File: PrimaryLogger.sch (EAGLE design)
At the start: 67 parts, among them J1 CONN_42.54_SCREW, J2 CONN_42.54_SCREW, J3 CONN_42.54_SCREW, J4 CONN_42.54_SCREW, J5 CONN_32.54_SCREW, Q1 DMG3404, Q2 DMG3404, U1 MIC2005, U2 MIC2091, U25 SN74AUP3G34DCU, U3 TPL5010DDC, U4 TXS0102DCU, U5 SN74LVC1G3157SC70, U6 TCS3400, U7 SHTC3DFN, U8 MCP23008QFN, U9 MCP7940SOIC

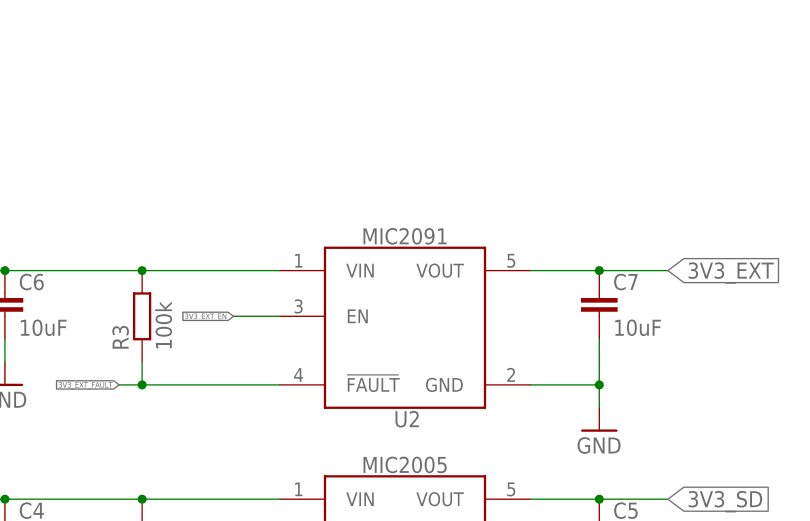
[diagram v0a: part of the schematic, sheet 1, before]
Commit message: Updated part numbers
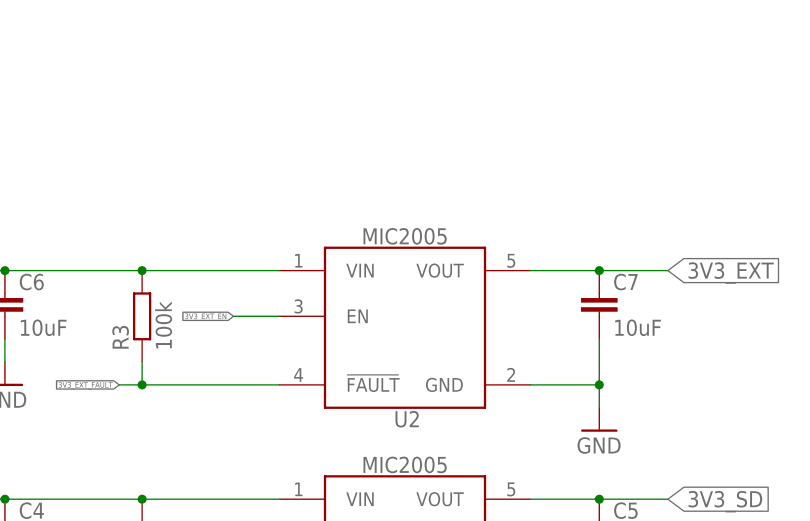
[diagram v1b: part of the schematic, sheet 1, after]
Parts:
- U2: value MIC2091 -> MIC2005; device bschulz:MIC2091 -> bschulz:MIC2005
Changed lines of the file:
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@@
 <part name="R2" library="bschulz_passives" deviceset="R-EU_" device="R0603" technology="100K" value="100k"/>
 <part name="GND7" library="supply1" library_urn="urn:adsk.eagle:library:371" deviceset="GND" device=""/>
-<part name="U2" library="bschulz" deviceset="MIC209*" device="" technology="1" value="MIC2091"/>
+<part name="U2" library="bschulz" deviceset="MIC2005" device="" value="MIC2005"/>
 <part name="C6" library="bschulz_passives" deviceset="C-EU" device="C0805" technology="10UF" value="10uF"/>
 <part name="C7" library="bschulz_passives" deviceset="C-EU" device="C0805" technology="10UF" value="10uF"/>

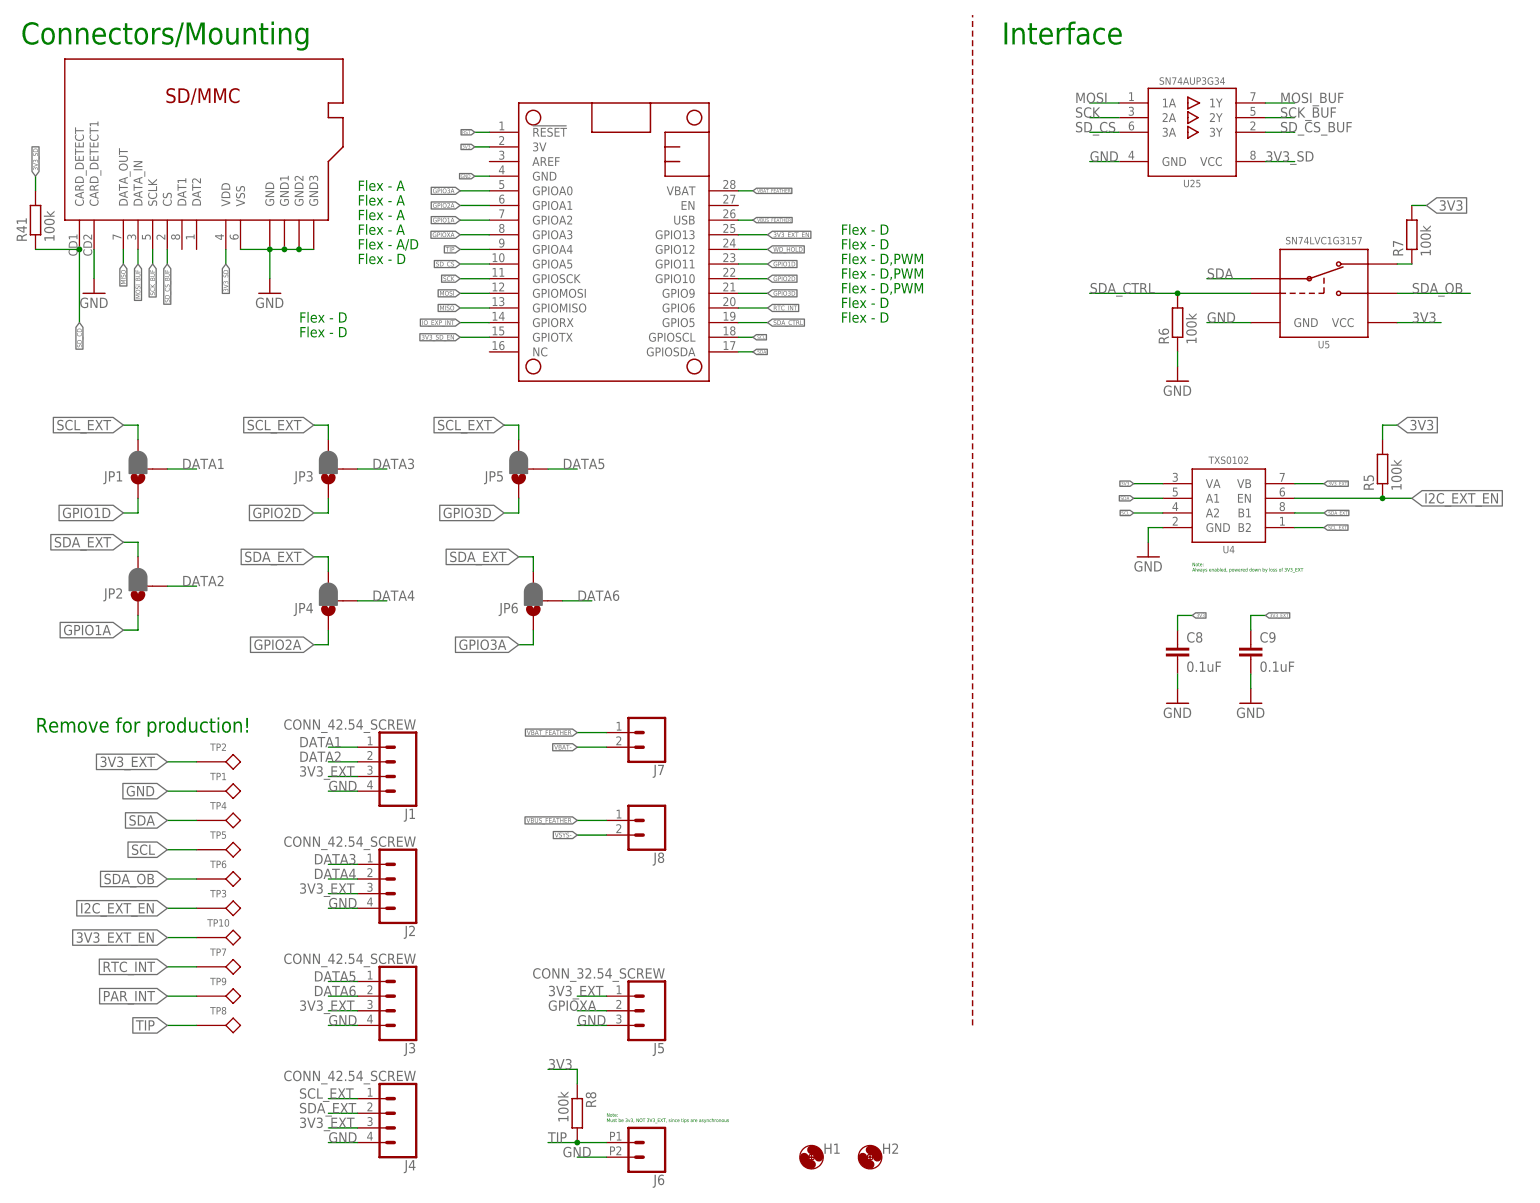
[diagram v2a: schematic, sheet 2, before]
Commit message: Updated parts for BoM, moved designators, changed R41
Updated part numbers to generate BoM, moved `R11` designator and changed `R41` to be `R12` to match ordering of rest of board (was carry over from Resnik I think)
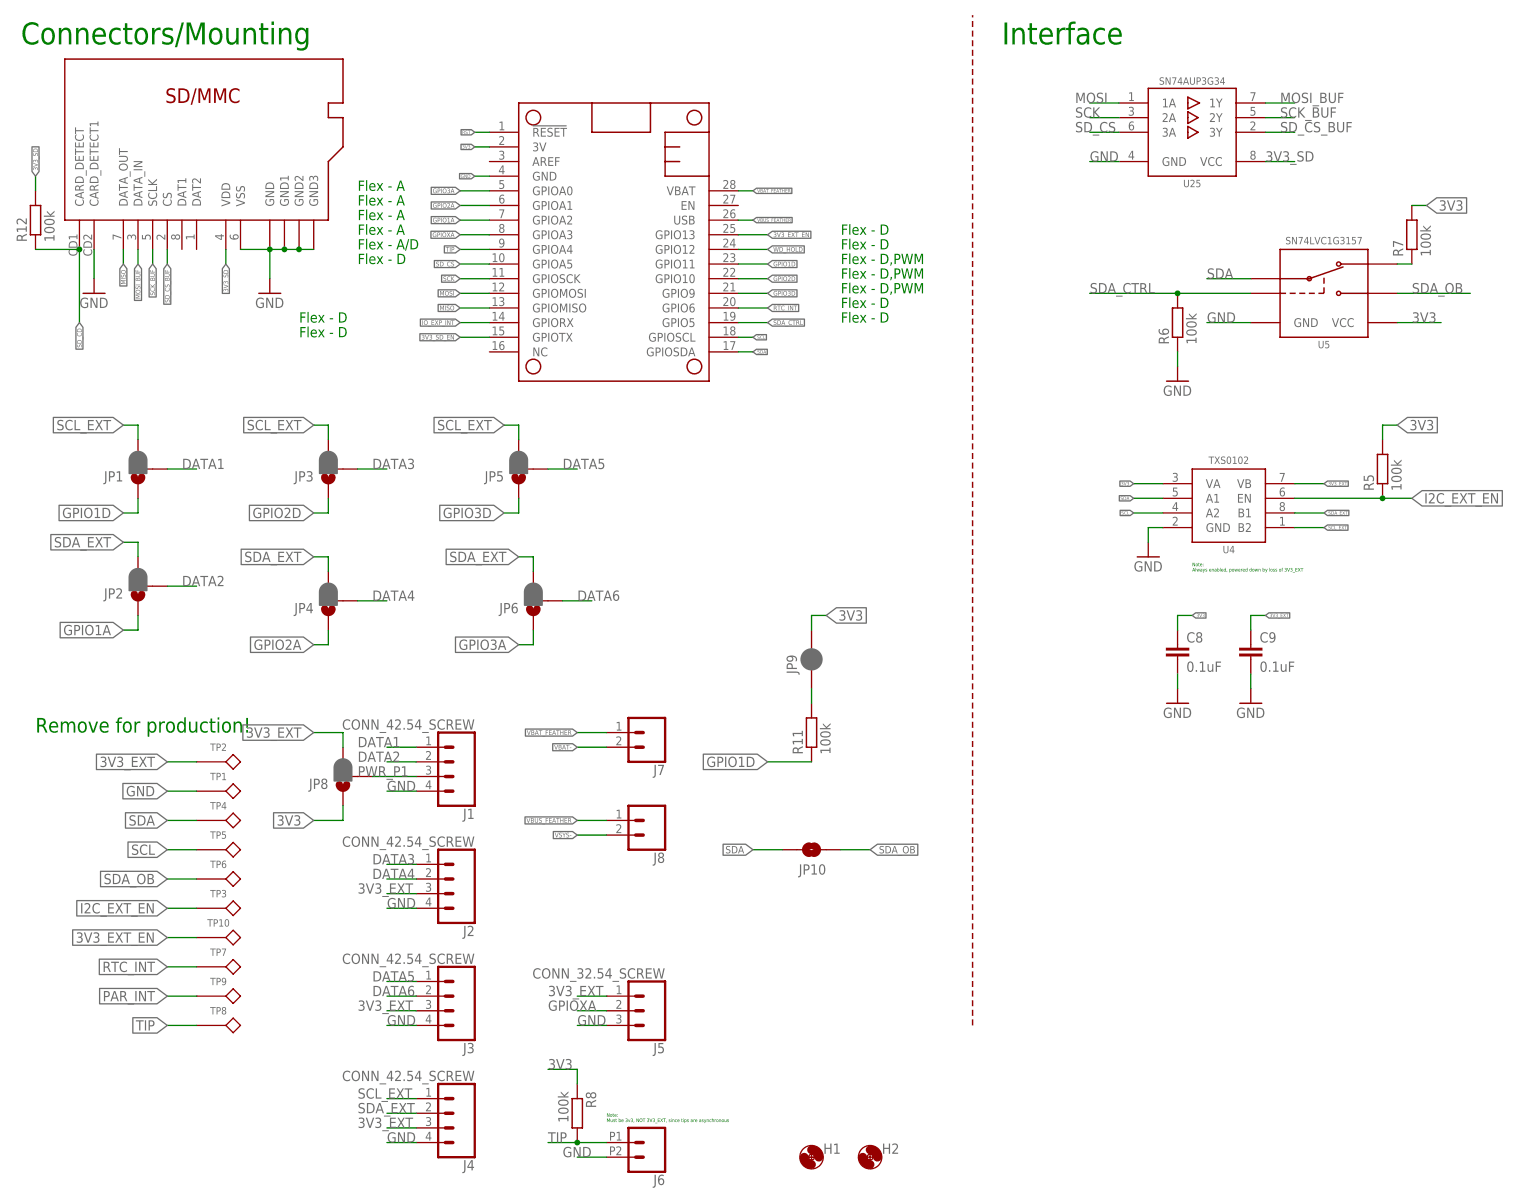
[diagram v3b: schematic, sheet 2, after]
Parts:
- added JP10: JUMPER-SMT_2_NO_SILK, SparkFun-Jumpers:JUMPER-SMT_2_NO_SILK
- added JP8: JUMPER-SMT_3_1-NC_PASTE_SILK, SparkFun-Jumpers:JUMPER-SMT_3_1-NC_PASTE_SILK
- added JP9: JUMPER-SMT_2_NC_PASTE_SILK, SparkFun-Jumpers:JUMPER-SMT_2_NC_PASTE_SILK
- added R11, R9: 100k, bschulz_passives:R-EU_100KR0603
- R8: device bschulz_passives:R-EU_100KR0603 -> bschulz_passives:R-EU_10KR0603
- renumbered R41 to R12
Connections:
- new net N$5: JP9.1, R11.2
- new net PWR_P1: J1.3, JP8.2
- net 3V3: now also JP8.1, JP9.2, R9.2
- net 3V3_EXT: now also JP8.3; no longer J1.3
- net GPIO1D: now also R11.1
- net RTC_INT: now also R9.1
- net SDA: now also JP10.2
- net SDA_OB: now also JP10.1
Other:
- moved on the sheet: J1, J2, J3, J4

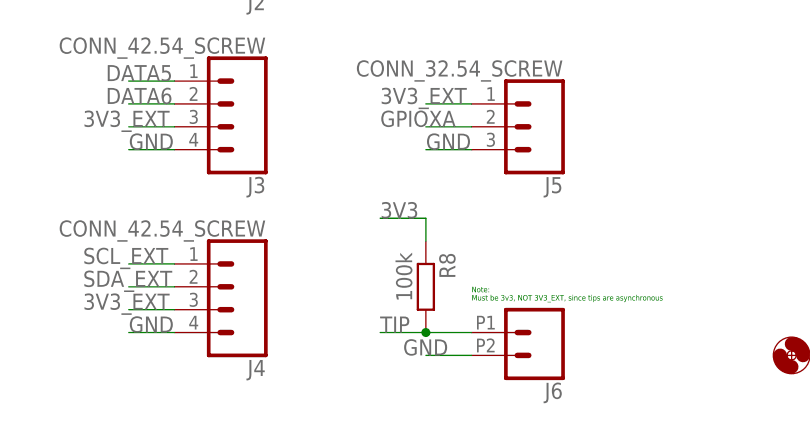
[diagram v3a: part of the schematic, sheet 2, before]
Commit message: Gerber and part updates
Added Gerber files for Advanced Circuits order, minor changes to part numbers and BoMs
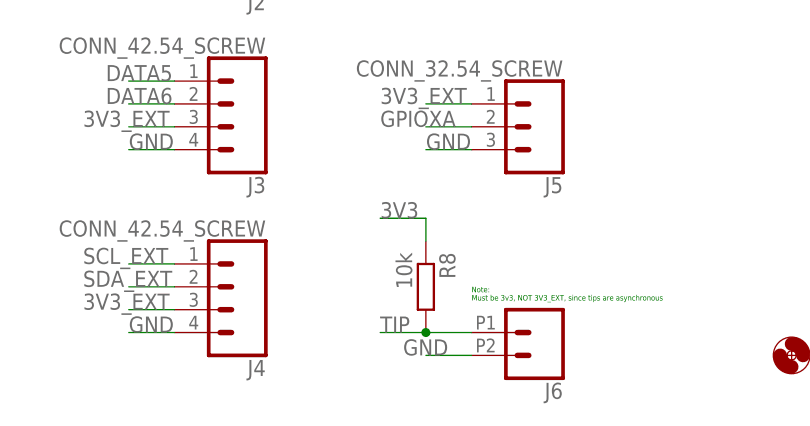
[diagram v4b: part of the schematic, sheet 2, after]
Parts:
- JP1, JP2, JP3, JP4, JP5, JP6, JP8: device SparkFun-Jumpers:JUMPER-SMT_3_1-NC_PASTE_SILK -> bschulz:JUMPER-SMT_3_1-NC_PASTE_SILK
- JP10: device SparkFun-Jumpers:JUMPER-SMT_2_NO_SILK -> bschulz:JUMPER-SMT_2_NO_SILK
- JP7, JP9: device SparkFun-Jumpers:JUMPER-SMT_2_NC_PASTE_SILK -> bschulz:JUMPER-SMT_2_NC_PASTE_SILK
- R8: value 100k -> 10k
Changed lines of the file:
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@@
 <?xml version="1.0" encoding="utf-8"?>
 <!DOCTYPE eagle SYSTEM "eagle.dtd">
-<eagle version="9.6.2">
+<eagle version="9.5.2">
 <drawing>
 <settings>
@@
 <layer number="115" name="ReferenceISLANDS" color="7" fill="1" visible="no" active="yes"/>
 <layer number="116" name="Patch_BOT" color="7" fill="1" visible="no" active="yes"/>
+<layer number="117" name="PM_Ref" color="7" fill="1" visible="no" active="no"/>
 <layer number="118" name="Rect_Pads" color="7" fill="1" visible="no" active="yes"/>
+<layer number="119" name="PF_Ref" color="7" fill="1" visible="no" active="no"/>
+<layer number="120" name="WFL_Ref" color="7" fill="1" visible="no" active="no"/>
 <layer number="121" name="_tsilk" color="7" fill="1" visible="no" active="yes"/>
 <layer number="122" name="_bsilk" color="7" fill="1" visible="no" active="yes"/>
@@
 <part name="J3" library="bschulz" deviceset="CONN_4" device="2.54_SCREW"/>
 <part name="J4" library="bschulz" deviceset="CONN_4" device="2.54_SCREW"/>
-<part name="JP1" library="SparkFun-Jumpers" library_urn="urn:adsk.eagle:library:528" deviceset="JUMPER-SMT_3_1-NC_PASTE" device="_SILK" package3d_urn="urn:adsk.eagle:package:39293/1"/>
-<part name="JP2" library="SparkFun-Jumpers" library_urn="urn:adsk.eagle:library:528" deviceset="JUMPER-SMT_3_1-NC_PASTE" device="_SILK" package3d_urn="urn:adsk.eagle:package:39293/1"/>
-<part name="JP3" library="SparkFun-Jumpers" library_urn="urn:adsk.eagle:library:528" deviceset="JUMPER-SMT_3_1-NC_PASTE" device="_SILK" package3d_urn="urn:adsk.eagle:package:39293/1"/>
-<part name="JP4" library="SparkFun-Jumpers" library_urn="urn:adsk.eagle:library:528" deviceset="JUMPER-SMT_3_1-NC_PASTE" device="_SILK" package3d_urn="urn:adsk.eagle:package:39293/1"/>
-<part name="JP5" library="SparkFun-Jumpers" library_urn="urn:adsk.eagle:library:528" deviceset="JUMPER-SMT_3_1-NC_PASTE" device="_SILK" package3d_urn="urn:adsk.eagle:package:39293/1"/>
-<part name="JP6" library="SparkFun-Jumpers" library_urn="urn:adsk.eagle:library:528" deviceset="JUMPER-SMT_3_1-NC_PASTE" device="_SILK" package3d_urn="urn:adsk.eagle:package:39293/1"/>
+<part name="JP1" library="bschulz" deviceset="JUMPER-SMT_3_1-NC_PASTE" device="_SILK" package3d_urn="urn:adsk.eagle:package:39293/1"/>
+<part name="JP2" library="bschulz" deviceset="JUMPER-SMT_3_1-NC_PASTE" device="_SILK" package3d_urn="urn:adsk.eagle:package:39293/1"/>
+<part name="JP3" library="bschulz" deviceset="JUMPER-SMT_3_1-NC_PASTE" device="_SILK" package3d_urn="urn:adsk.eagle:package:39293/1"/>
+<part name="JP4" library="bschulz" deviceset="JUMPER-SMT_3_1-NC_PASTE" device="_SILK" package3d_urn="urn:adsk.eagle:package:39293/1"/>
+<part name="JP5" library="bschulz" deviceset="JUMPER-SMT_3_1-NC_PASTE" device="_SILK" package3d_urn="urn:adsk.eagle:package:39293/1"/>
+<part name="JP6" library="bschulz" deviceset="JUMPER-SMT_3_1-NC_PASTE" device="_SILK" package3d_urn="urn:adsk.eagle:package:39293/1"/>
 <part name="U5" library="bschulz" deviceset="SN74LVC1G3157" device="SC70" value="SN74LVC1G3157SC70"/>
 <part name="R6" library="bschulz_passives" deviceset="R-EU_" device="R0603" technology="100K" value="100k"/>
@@
 <part name="J5" library="bschulz" deviceset="CONN_3" device="2.54_SCREW"/>
 <part name="J6" library="bschulz" deviceset="CONN_02" device="2.54_SCREW_ROUND"/>
-<part name="R8" library="bschulz_passives" deviceset="R-EU_" device="R0603" technology="10K" value="100k"/>
+<part name="R8" library="bschulz_passives" deviceset="R-EU_" device="R0603" technology="10K" value="10k"/>
 <part name="J7" library="bschulz" deviceset="CONN_02" device="3.5MM_ROUND"/>
 <part name="J8" library="bschulz" deviceset="CONN_02" device="3.5MM_ROUND"/>
@@
 </part>
 <part name="C14" library="bschulz_passives" deviceset="C-EU" device="C0603" technology="0.1UF" value="0.1uF"/>
-<part name="JP7" library="SparkFun-Jumpers" library_urn="urn:adsk.eagle:library:528" deviceset="JUMPER-SMT_2_NC_PASTE" device="_SILK" package3d_urn="urn:adsk.eagle:package:39282/1"/>
+<part name="JP7" library="bschulz" deviceset="JUMPER-SMT_2_NC_PASTE" device="_SILK" package3d_urn="urn:adsk.eagle:package:39282/1"/>
 <part name="GND23" library="supply1" library_urn="urn:adsk.eagle:library:371" deviceset="GND" device=""/>
 <part name="R9" library="bschulz_passives" deviceset="R-EU_" device="R0603" technology="100K" value="100k"/>
-<part name="JP8" library="SparkFun-Jumpers" library_urn="urn:adsk.eagle:library:528" deviceset="JUMPER-SMT_3_1-NC_PASTE" device="_SILK" package3d_urn="urn:adsk.eagle:package:39293/1"/>
+<part name="JP8" library="bschulz" deviceset="JUMPER-SMT_3_1-NC_PASTE" device="_SILK" package3d_urn="urn:adsk.eagle:package:39293/1"/>
 <part name="R11" library="bschulz_passives" deviceset="R-EU_" device="R0603" technology="100K" value="100k"/>
-<part name="JP9" library="SparkFun-Jumpers" library_urn="urn:adsk.eagle:library:528" deviceset="JUMPER-SMT_2_NC_PASTE" device="_SILK" package3d_urn="urn:adsk.eagle:package:39282/1"/>
-<part name="JP10" library="SparkFun-Jumpers" library_urn="urn:adsk.eagle:library:528" deviceset="JUMPER-SMT_2_NO" device="_SILK" package3d_urn="urn:adsk.eagle:package:39279/1"/>
+<part name="JP9" library="bschulz" deviceset="JUMPER-SMT_2_NC_PASTE" device="_SILK" package3d_urn="urn:adsk.eagle:package:39282/1"/>
+<part name="JP10" library="bschulz" deviceset="JUMPER-SMT_2_NO" device="_SILK" package3d_urn="urn:adsk.eagle:package:39279/1"/>
 </parts>
 <sheets>
